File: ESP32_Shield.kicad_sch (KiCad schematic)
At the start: 36 parts, among them J1 BME280, SHT40 Module, J10 SCD40 Module, J11 Conn_01x03, J12 Conn_01x03, J13 SCD40 Module, J14 BME280, SHT40 Module, J2 SCD40 Module, J3 Conn_01x02, J4 Qwiic_Vertical, J5 Conn_01x02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

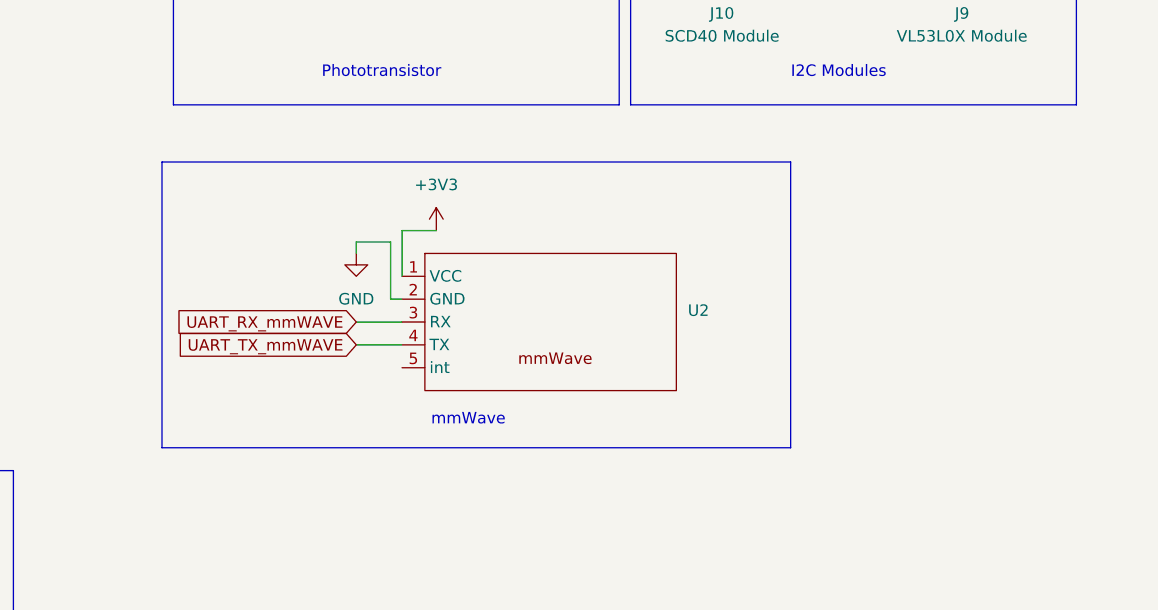
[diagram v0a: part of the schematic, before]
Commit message: add silk screen and mmWave connector
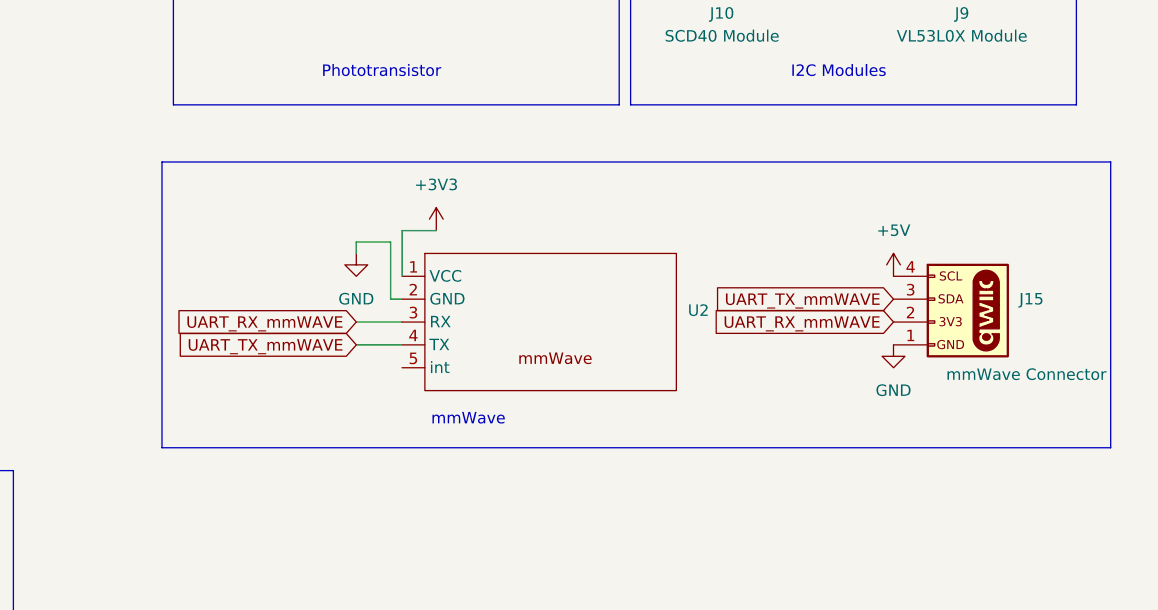
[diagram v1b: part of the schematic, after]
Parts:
- added J15: mmWave Connector, PCM_SparkFun-Connector:JST_1x04_P1.0mm_Vertical_SMD, symbol PCM_SparkFun-Connector:Qwiic_Vertical
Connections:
- net +5V: now also J15.4 (Pin_4)
- net GND: now also J15.1 (Pin_1)
- net UART_RX_mmWAVE: now also J15.2 (Pin_2)
- net UART_TX_mmWAVE: now also J15.3 (Pin_3)
- new net: J15.NC1 (NC), J15.NC2 (NC)

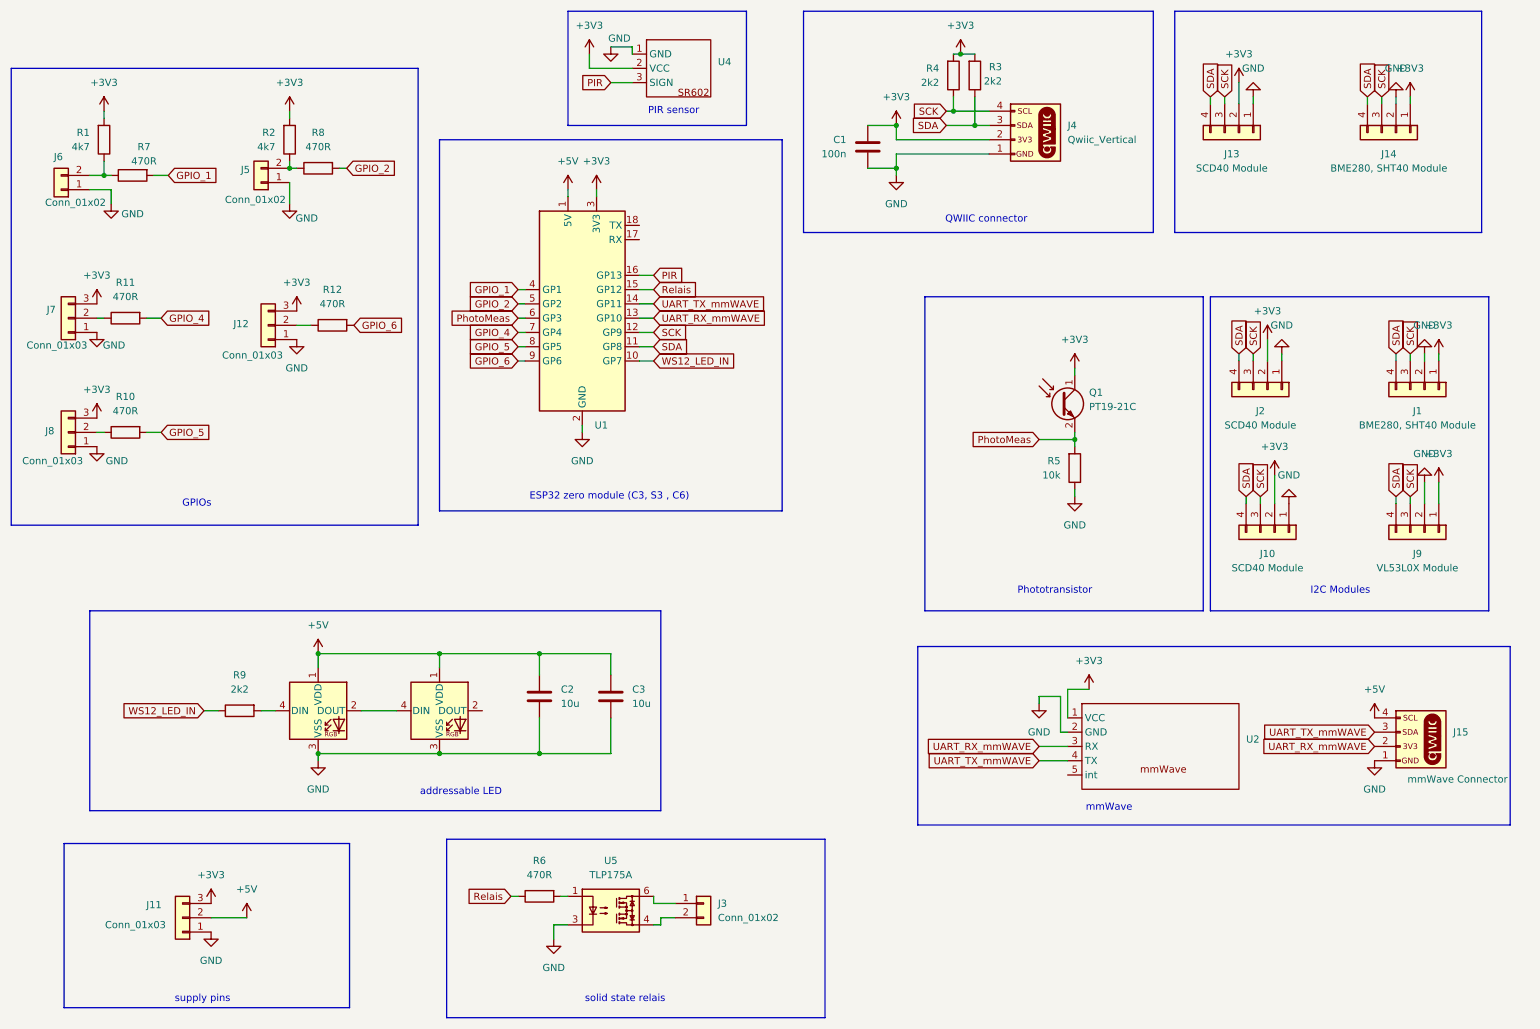
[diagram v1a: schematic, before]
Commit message: add more JST connectors for UART
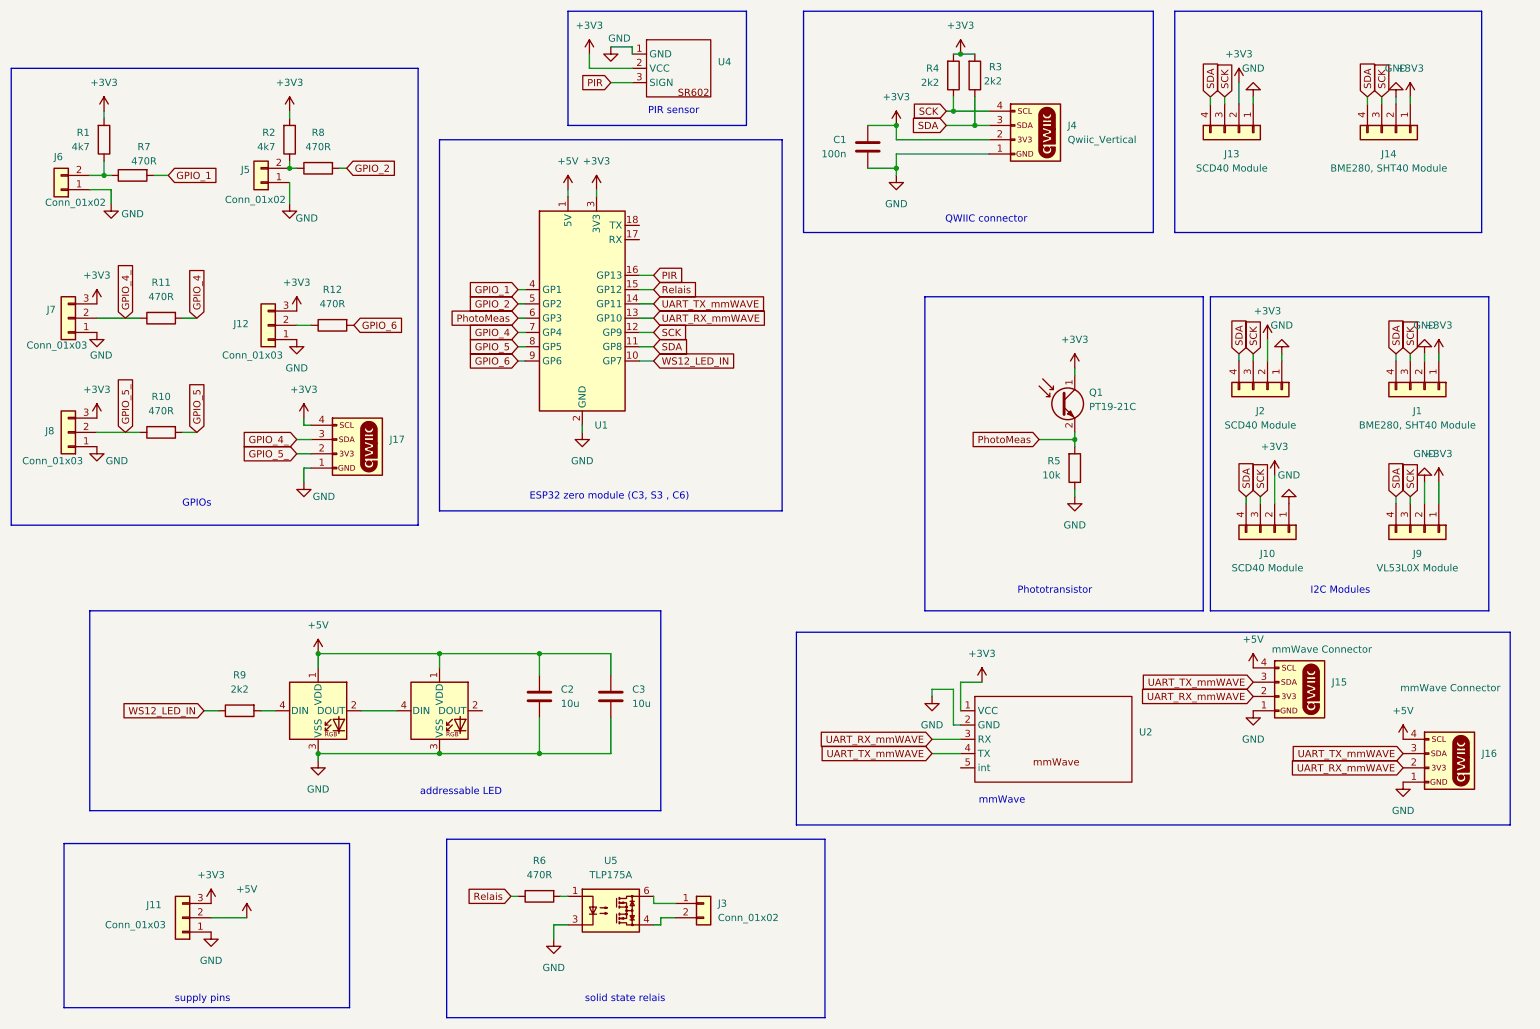
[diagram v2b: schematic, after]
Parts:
- added J16, J17: mmWave Connector, PCM_SparkFun-Connector:JST_1x04_P1.0mm_Vertical_SMD, symbol PCM_SparkFun-Connector:Qwiic_Vertical
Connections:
- net +3V3: now also J17.4 (Pin_4)
- net +5V: now also J16.4 (Pin_4)
- net GND: now also J16.1 (Pin_1), J17.1 (Pin_1)
- net UART_RX_mmWAVE: now also J16.2 (Pin_2)
- net UART_TX_mmWAVE: now also J16.3 (Pin_3)
- net GPIO_5_: now reaches J8.2 (Pin_2), R10.1
- net GPIO_5_: now also J17.2 (Pin_2)
- net GPIO_4_: now reaches J7.2 (Pin_2), R11.1
- net GPIO_4_: now also J17.3 (Pin_3)
- new net: J17.NC1 (NC), J17.NC2 (NC)
- new net: J16.NC1 (NC), J16.NC2 (NC)
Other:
- moved on the sheet: J15, R10, R11, U2

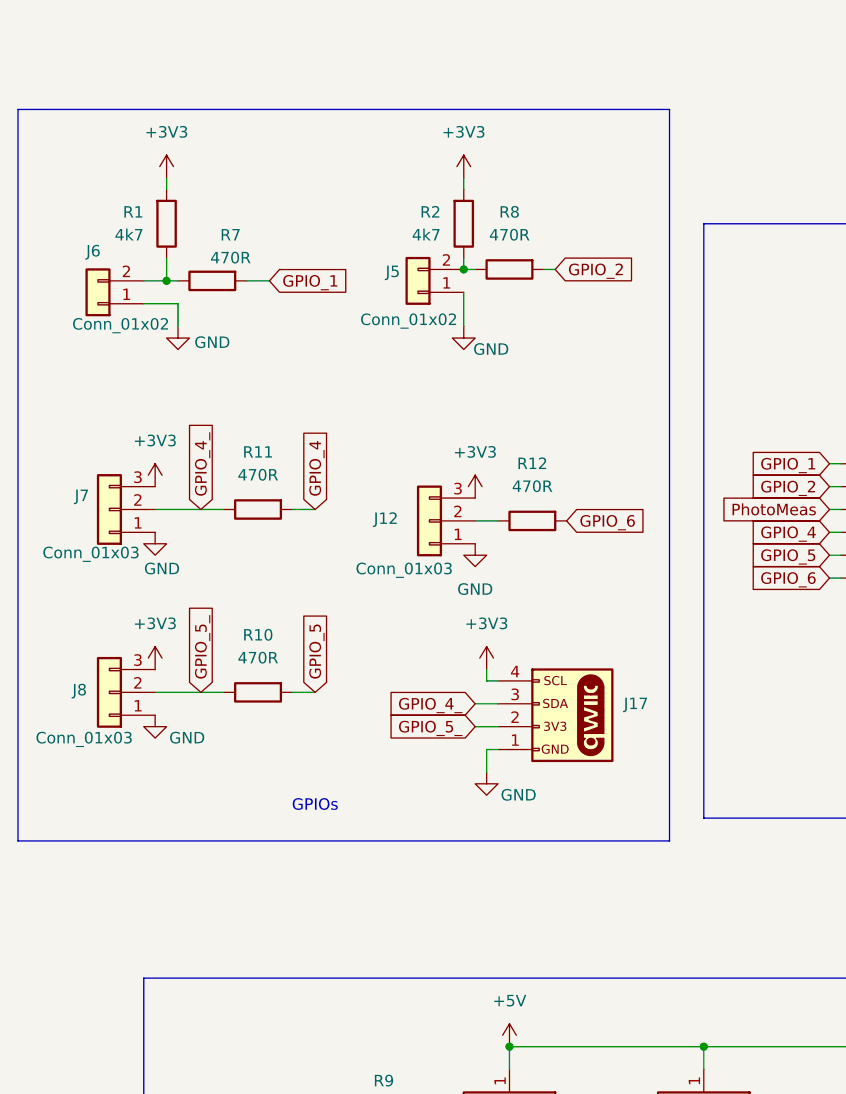
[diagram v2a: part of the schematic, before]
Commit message: add jst connector for aditional gpios
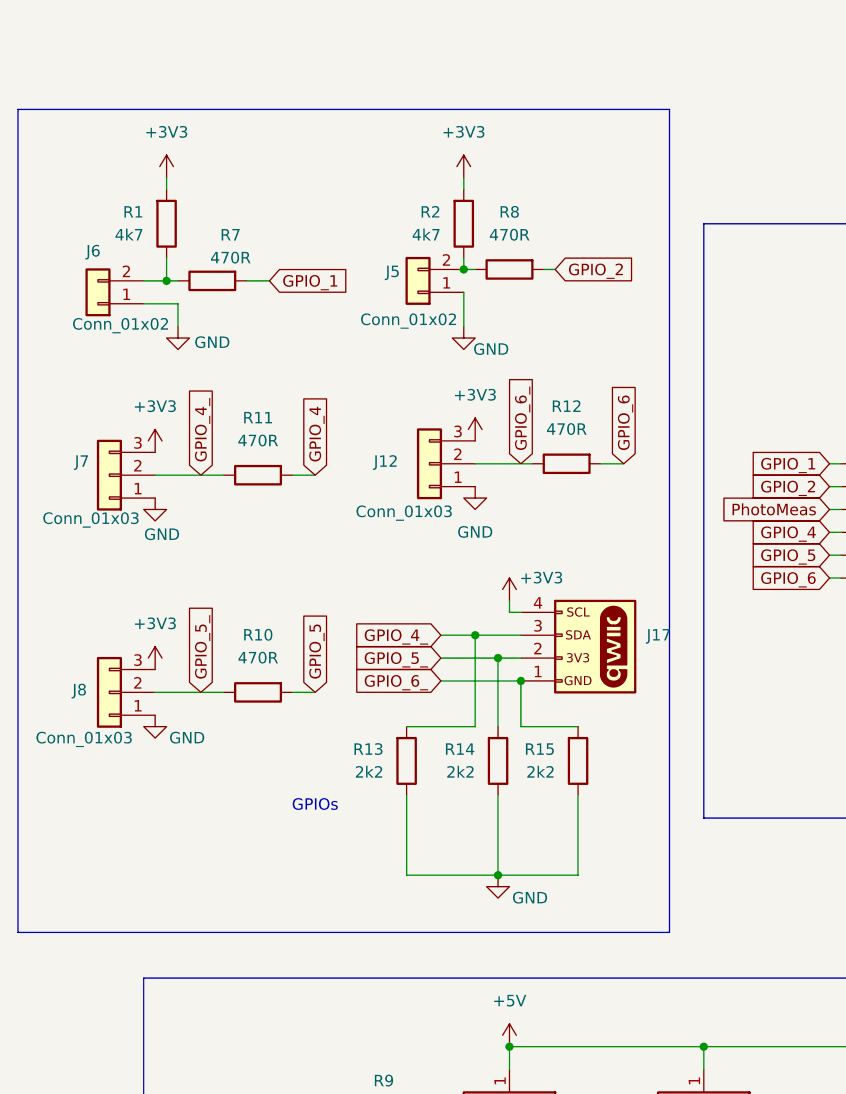
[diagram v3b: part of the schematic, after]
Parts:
- added R13, R14, R15: 2k2, Resistor_SMD:R_0805_2012Metric, symbol Device:R
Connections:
- net GND: now also R13.1, R14.1, R15.1; no longer J17.1 (Pin_1)
- net GPIO_4_: now also R13.2
- net GPIO_5_: now also R14.2
- net GPIO_6_: now reaches J12.2 (Pin_2), R12.1
- net GPIO_6_: now also J17.1 (Pin_1), R15.2
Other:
- moved on the sheet: J12, J17, J7, R11, R12
